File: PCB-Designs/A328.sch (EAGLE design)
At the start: 15 parts

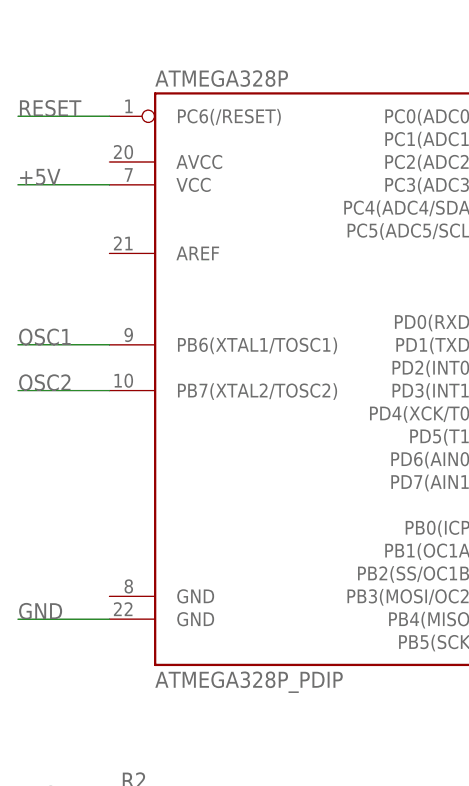
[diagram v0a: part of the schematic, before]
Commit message: Smaller board, redundant power according to arduino schematic.
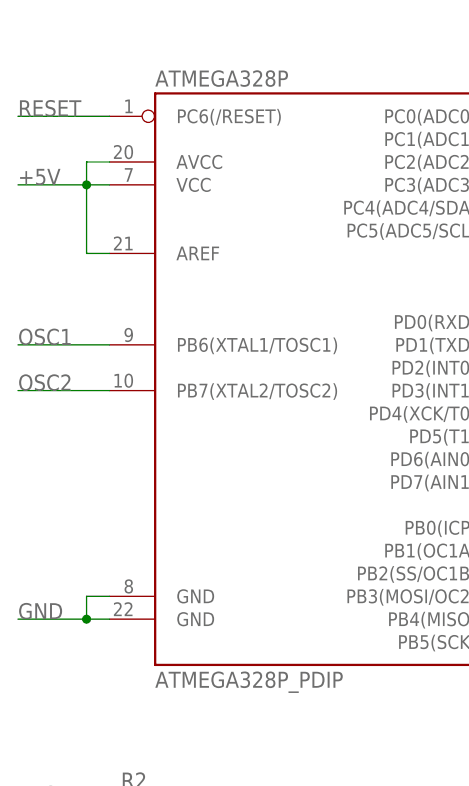
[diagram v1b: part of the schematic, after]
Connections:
- net +5V: now also ATMEGA328P.AREF, ATMEGA328P.AVCC
- net GND: now also ATMEGA328P.GND@1
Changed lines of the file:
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@@
 <segment>
 <pinref part="ATMEGA328P" gate="G$1" pin="GND@2"/>
-<wire x1="-10.16" y1="30.48" x2="-20.32" y2="30.48" width="0.1524" layer="91"/>
+<wire x1="-10.16" y1="30.48" x2="-12.7" y2="30.48" width="0.1524" layer="91"/>
 <label x="-20.32" y="30.48" size="1.778" layer="95"/>
+<pinref part="ATMEGA328P" gate="G$1" pin="GND@1"/>
+<wire x1="-12.7" y1="30.48" x2="-20.32" y2="30.48" width="0.1524" layer="91"/>
+<wire x1="-10.16" y1="33.02" x2="-12.7" y2="33.02" width="0.1524" layer="91"/>
+<wire x1="-12.7" y1="33.02" x2="-12.7" y2="30.48" width="0.1524" layer="91"/>
+<junction x="-12.7" y="30.48"/>
 </segment>
 <segment>
@@
 <segment>
 <pinref part="ATMEGA328P" gate="G$1" pin="VCC"/>
-<wire x1="-10.16" y1="78.74" x2="-20.32" y2="78.74" width="0.1524" layer="91"/>
+<wire x1="-10.16" y1="78.74" x2="-12.7" y2="78.74" width="0.1524" layer="91"/>
 <label x="-20.32" y="78.74" size="1.778" layer="95"/>
+<pinref part="ATMEGA328P" gate="G$1" pin="AVCC"/>
+<wire x1="-12.7" y1="78.74" x2="-20.32" y2="78.74" width="0.1524" layer="91"/>
+<wire x1="-10.16" y1="81.28" x2="-12.7" y2="81.28" width="0.1524" layer="91"/>
+<wire x1="-12.7" y1="81.28" x2="-12.7" y2="78.74" width="0.1524" layer="91"/>
+<junction x="-12.7" y="78.74"/>
+<pinref part="ATMEGA328P" gate="G$1" pin="AREF"/>
+<wire x1="-10.16" y1="71.12" x2="-12.7" y2="71.12" width="0.1524" layer="91"/>
+<wire x1="-12.7" y1="71.12" x2="-12.7" y2="78.74" width="0.1524" layer="91"/>
 </segment>
 <segment>
